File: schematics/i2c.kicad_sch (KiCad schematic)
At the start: 15 parts, among them U35 PCA9306D_SOIC, U36 M24C64-F_DFN8

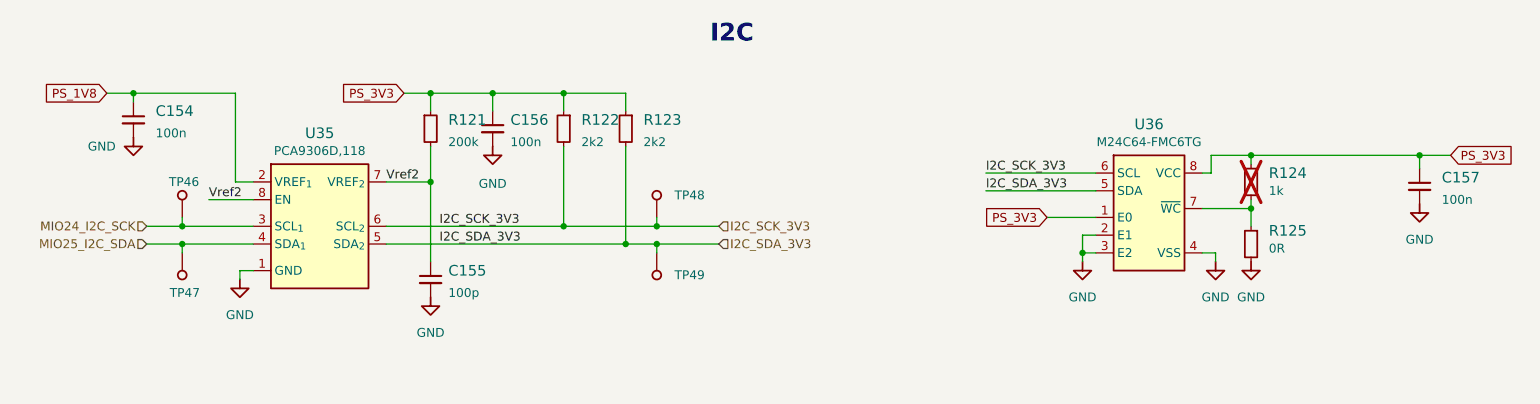
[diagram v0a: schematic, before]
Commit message: Voltage converter added
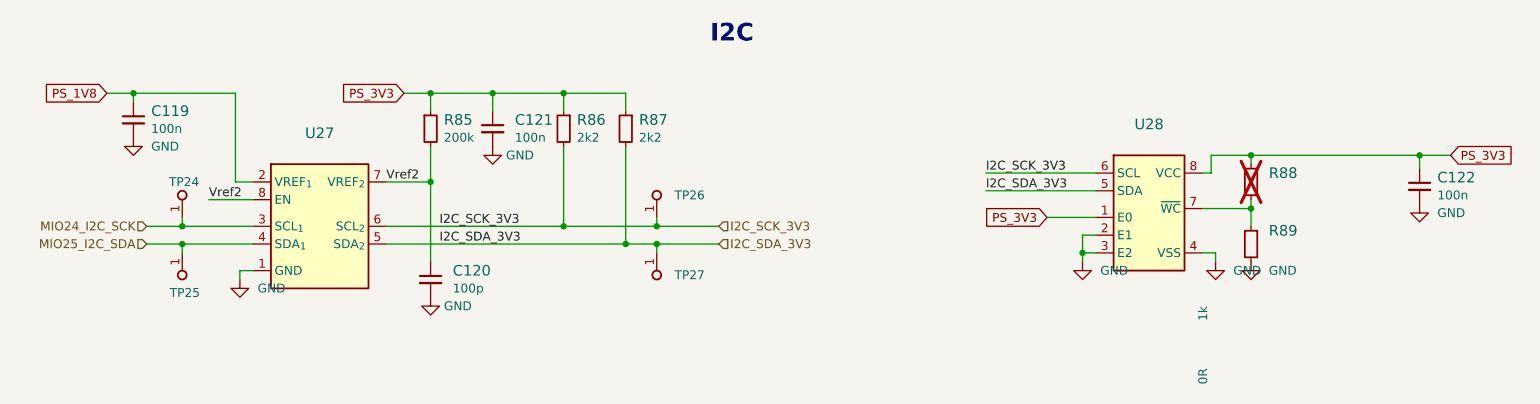
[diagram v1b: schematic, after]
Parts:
- R89: renamed from R125; DNP DNP -> (none); now in the parts list
- TP24: renamed from TP46; now left out of the parts list
- TP25: renamed from TP47; now left out of the parts list
- TP26: renamed from TP48; now left out of the parts list
- TP27: renamed from TP49; now left out of the parts list
- renumbered C154 to C119, C155 to C120, C156 to C121, C157 to C122, R121 to R85, R122 to R86, R123 to R87, R124 to R88, U35 to U27, U36 to U28
